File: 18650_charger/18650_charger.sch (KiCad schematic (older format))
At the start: 19 parts

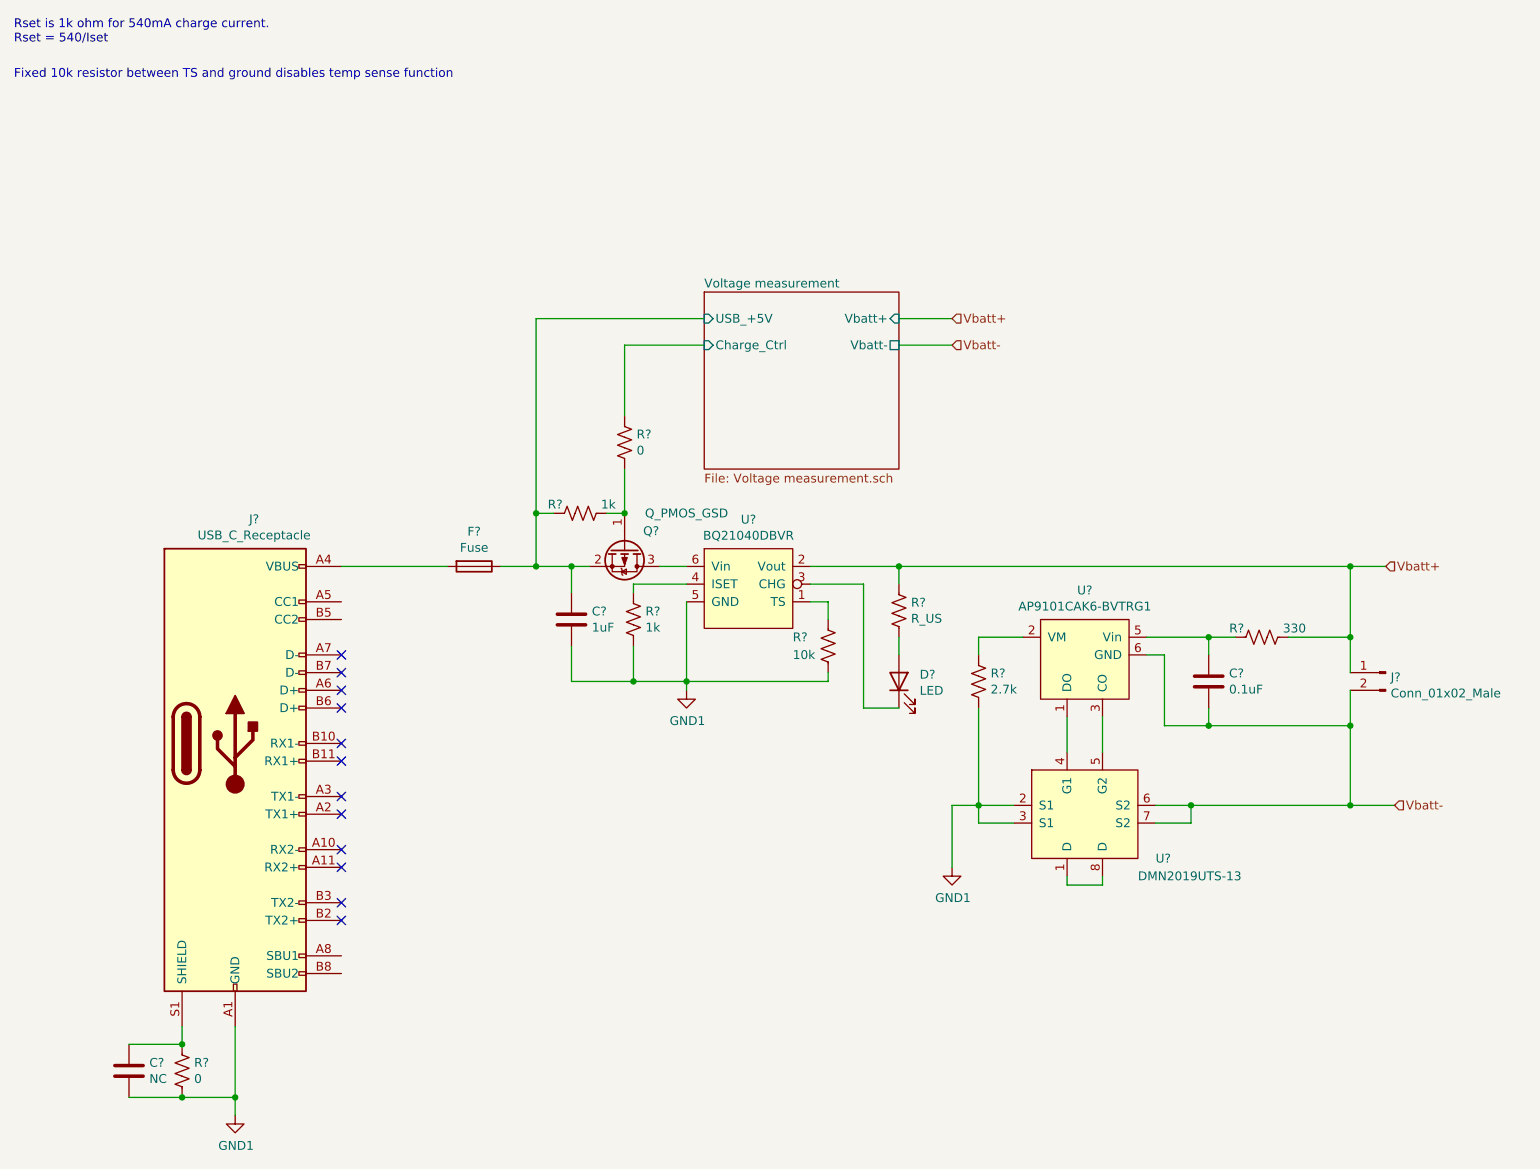
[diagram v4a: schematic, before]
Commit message: Updated STM32 schematic
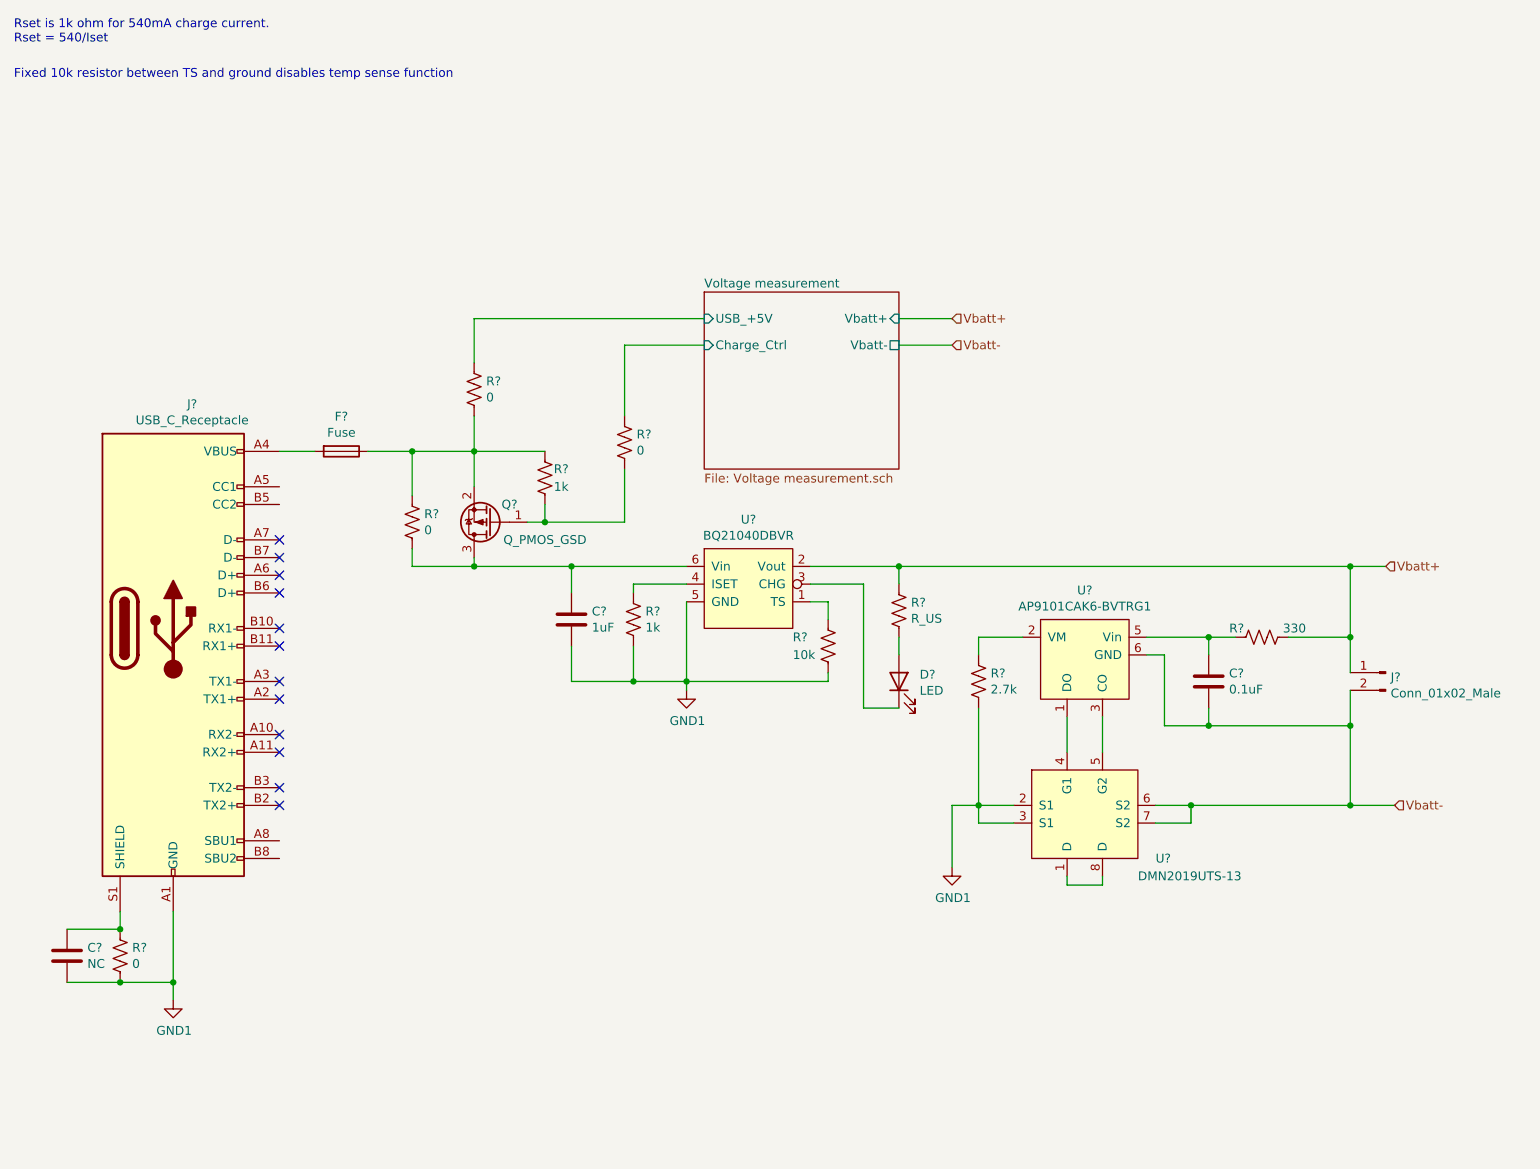
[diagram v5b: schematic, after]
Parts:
- added R? (x2): 0, symbol Device:R_US
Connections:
- net Voltage measurement/USB_+5V: now also R?.1; no longer C?.1, F?.1, Q?.2 (S), R?.1
- net at Q?.3 (D), U?.6 (Vin): now also C?.1, R?.2
- new net: F?.1, Q?.2 (S), R?.1, R?.1, R?.2
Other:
- moved on the sheet: C?, F?, J?, Q?, R?
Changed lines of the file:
@@
 L Connector:USB_C_Receptacle J?
 U 1 1 5F267AF4
-P 2050 4850
-F 0 "J?" H 2157 6117 50  0000 C CNN
-F 1 "USB_C_Receptacle" H 2157 6026 50  0000 C CNN
-F 2 "" H 2200 4850 50  0001 C CNN
-F 3 "https://www.usb.org/sites/default/files/documents/usb_type-c.zip" H 2200 4850 50  0001 C CNN
-	1    2050 4850
+P 1700 4200
+F 0 "J?" H 1807 5467 50  0000 C CNN
+F 1 "USB_C_Receptacle" H 1807 5376 50  0000 C CNN
+F 2 "" H 1850 4200 50  0001 C CNN
+F 3 "https://www.usb.org/sites/default/files/documents/usb_type-c.zip" H 1850 4200 50  0001 C CNN
+	1    1700 4200
 	1    0    0    -1
 $EndComp
@@
 Text Notes 800  900  0    50   ~ 0
 Rset is 1k ohm for 540mA charge current.\nRset = 540/Iset
-NoConn ~ 2650 5850
-NoConn ~ 2650 5750
-NoConn ~ 2650 5550
-NoConn ~ 2650 5450
-NoConn ~ 2650 5250
-NoConn ~ 2650 5150
-NoConn ~ 2650 4950
-NoConn ~ 2650 4850
-NoConn ~ 2650 4650
-NoConn ~ 2650 4550
-NoConn ~ 2650 4450
-NoConn ~ 2650 4350
+NoConn ~ 2300 5200
+NoConn ~ 2300 5100
+NoConn ~ 2300 4900
+NoConn ~ 2300 4800
+NoConn ~ 2300 4600
+NoConn ~ 2300 4500
+NoConn ~ 2300 4300
+NoConn ~ 2300 4200
+NoConn ~ 2300 4000
+NoConn ~ 2300 3900
+NoConn ~ 2300 3800
+NoConn ~ 2300 3700
 Text Notes 800  1100 0    50   ~ 0
 Fixed 10k resistor between TS and ground disables temp sense function
@@
 	-1   0    0    -1
 $EndComp
-Wire Wire Line
-	3750 3850 3950 3850
 Wire Wire Line
 	4600 3950 4300 3950
@@
 L Device:Fuse F?
 U 1 1 5F26A8E6
-P 3400 3850
-F 0 "F?" V 3203 3850 50  0000 C CNN
-F 1 "Fuse" V 3294 3850 50  0000 C CNN
-F 2 "" V 3330 3850 50  0001 C CNN
-F 3 "~" H 3400 3850 50  0001 C CNN
-	1    3400 3850
+P 2650 3200
+F 0 "F?" V 2453 3200 50  0000 C CNN
+F 1 "Fuse" V 2544 3200 50  0000 C CNN
+F 2 "" V 2580 3200 50  0001 C CNN
+F 3 "~" H 2650 3200 50  0001 C CNN
+	1    2650 3200
 	0    1    1    0
 $EndComp
 Wire Wire Line
-	3950 3850 3950 4000
-Wire Wire Line
 	3950 4500 3950 4300
-Wire Wire Line
-	4050 3850 3950 3850
-Connection ~ 3950 3850
-Wire Wire Line
-	4450 3850 4600 3850
-Wire Wire Line
-	3750 3850 3750 3550
-Wire Wire Line
-	3750 3550 3850 3550
-Wire Wire Line
-	3550 3850 3750 3850
-Connection ~ 3750 3850
 $Comp
 L Device:R_US R?
@@
 	4250 2600 4250 3000
 Wire Wire Line
-	3750 3550 3750 2450
-Wire Wire Line
-	3750 2450 4700 2450
-Connection ~ 3750 3550
-Wire Wire Line
 	5800 2450 6100 2450
 Wire Wire Line
@@
 Text HLabel 6100 2600 2    50   Input ~ 0
 Vbatt-
-Wire Wire Line
-	3250 3850 2650 3850
 $Comp
 L Device:Q_PMOS_GSD Q?
 U 1 1 5F42065E
-P 4250 3750
-F 0 "Q?" V 4150 3900 50  0000 C CNN
-F 1 "Q_PMOS_GSD" V 4050 4100 50  0000 C CNN
-F 2 "" H 4450 3850 50  0001 C CNN
-F 3 "~" H 4250 3750 50  0001 C CNN
-	1    4250 3750
-	0    1    1    0
+P 3500 3600
+F 0 "Q?" H 3400 3500 50  0000 C CNN
+F 1 "Q_PMOS_GSD" H 3200 3700 50  0000 C CNN
+F 2 "" H 3700 3700 50  0001 C CNN
+F 3 "~" H 3500 3600 50  0001 C CNN
+	1    3500 3600
+	-1   0    0    1
 $EndComp
 $Comp
 L Device:R_US R?
 U 1 1 5F3A1849
-P 4000 3550
-F 0 "R?" V 4050 3650 50  0000 L CNN
-F 1 "1k" V 4050 3350 50  0000 L CNN
-F 2 "" V 4040 3540 50  0001 C CNN
-F 3 "~" H 4000 3550 50  0001 C CNN
-	1    4000 3550
-	0    -1   -1   0
-$EndComp
-Wire Wire Line
-	4150 3550 4250 3550
-Wire Wire Line
-	4250 3300 4250 3550
-Connection ~ 4250 3550
+P 3800 3350
+F 0 "R?" H 3850 3400 50  0000 L CNN
+F 1 "1k" H 3850 3300 50  0000 L CNN
+F 2 "" V 3840 3340 50  0001 C CNN
+F 3 "~" H 3800 3350 50  0001 C CNN
+	1    3800 3350
+	1    0    0    -1
+$EndComp
 $Comp
 L power:GND1 #PWR?
@@
 L power:GND1 #PWR?
 U 1 1 5F3D2AF9
-P 2050 6950
-F 0 "#PWR?" H 2050 6700 50  0001 C CNN
-F 1 "GND1" H 2055 6777 50  0000 C CNN
-F 2 "" H 2050 6950 50  0001 C CNN
-F 3 "" H 2050 6950 50  0001 C CNN
-	1    2050 6950
+P 1700 6300
+F 0 "#PWR?" H 1700 6050 50  0001 C CNN
+F 1 "GND1" H 1705 6127 50  0000 C CNN
+F 2 "" H 1700 6300 50  0001 C CNN
+F 3 "" H 1700 6300 50  0001 C CNN
+	1    1700 6300
 	1    0    0    -1
 $EndComp
@@
 L Device:R_US R?
 U 1 1 5F3D37C0
-P 1750 6700
-F 0 "R?" H 1818 6746 50  0000 L CNN
-F 1 "0" H 1818 6655 50  0000 L CNN
-F 2 "" V 1790 6690 50  0001 C CNN
-F 3 "~" H 1750 6700 50  0001 C CNN
-	1    1750 6700
+P 1400 6050
+F 0 "R?" H 1468 6096 50  0000 L CNN
+F 1 "0" H 1468 6005 50  0000 L CNN
+F 2 "" V 1440 6040 50  0001 C CNN
+F 3 "~" H 1400 6050 50  0001 C CNN
+	1    1400 6050
 	1    0    0    -1
 $EndComp
@@
 L Device:C C?
 U 1 1 5F3D5BC2
-P 1450 6700
-F 0 "C?" H 1565 6746 50  0000 L CNN
-F 1 "NC" H 1565 6655 50  0000 L CNN
-F 2 "" H 1488 6550 50  0001 C CNN
-F 3 "~" H 1450 6700 50  0001 C CNN
-	1    1450 6700
-	1    0    0    -1
-$EndComp
-Wire Wire Line
-	1450 6550 1750 6550
-Wire Wire Line
-	1750 6550 1750 6450
-Connection ~ 1750 6550
-Wire Wire Line
-	1450 6850 1750 6850
-Wire Wire Line
-	1750 6850 2050 6850
-Wire Wire Line
-	2050 6850 2050 6950
-Connection ~ 1750 6850
-Wire Wire Line
-	2050 6450 2050 6850
-Connection ~ 2050 6850
+P 1100 6050
+F 0 "C?" H 1215 6096 50  0000 L CNN
+F 1 "NC" H 1215 6005 50  0000 L CNN
+F 2 "" H 1138 5900 50  0001 C CNN
+F 3 "~" H 1100 6050 50  0001 C CNN
+	1    1100 6050
+	1    0    0    -1
+$EndComp
+Wire Wire Line
+	1100 5900 1400 5900
+Wire Wire Line
+	1400 5900 1400 5800
+Connection ~ 1400 5900
+Wire Wire Line
+	1100 6200 1400 6200
+Wire Wire Line
+	1400 6200 1700 6200
+Wire Wire Line
+	1700 6200 1700 6300
+Connection ~ 1400 6200
+Wire Wire Line
+	1700 5800 1700 6200
+Connection ~ 1700 6200
+$Comp
+L Device:R_US R?
+U 1 1 5F418CD0
+P 3050 3600
+F 0 "R?" H 3118 3646 50  0000 L CNN
+F 1 "0" H 3118 3555 50  0000 L CNN
+F 2 "" V 3090 3590 50  0001 C CNN
+F 3 "~" H 3050 3600 50  0001 C CNN
+	1    3050 3600
+	1    0    0    -1
+$EndComp
+Wire Wire Line
+	3400 3850 3400 3800
+Wire Wire Line
+	3400 3850 3950 3850
+Wire Wire Line
+	3400 3850 3050 3850
+Wire Wire Line
+	3050 3850 3050 3750
+Connection ~ 3400 3850
+Wire Wire Line
+	3400 3400 3400 3200
+Wire Wire Line
+	3400 3200 3050 3200
+Wire Wire Line
+	3050 3450 3050 3200
+Connection ~ 3050 3200
+Wire Wire Line
+	3050 3200 2800 3200
+Wire Wire Line
+	3400 3200 3800 3200
+Connection ~ 3400 3200
+Wire Wire Line
+	3400 2450 4700 2450
+Wire Wire Line
+	3800 3500 3800 3600
+Wire Wire Line
+	3800 3600 3700 3600
+Wire Wire Line
+	4250 3300 4250 3600
+Wire Wire Line
+	4250 3600 3800 3600
+Connection ~ 3800 3600
+Wire Wire Line
+	2300 3200 2500 3200
+Wire Wire Line
+	3950 4000 3950 3850
+Connection ~ 3950 3850
+Wire Wire Line
+	3950 3850 4600 3850
+$Comp
+L Device:R_US R?
+U 1 1 5F439837
+P 3400 2850
+F 0 "R?" H 3468 2896 50  0000 L CNN
+F 1 "0" H 3468 2805 50  0000 L CNN
+F 2 "" V 3440 2840 50  0001 C CNN
+F 3 "~" H 3400 2850 50  0001 C CNN
+	1    3400 2850
+	1    0    0    -1
+$EndComp
+Wire Wire Line
+	3400 3200 3400 3000
+Wire Wire Line
+	3400 2450 3400 2700
 $EndSCHEMATC
